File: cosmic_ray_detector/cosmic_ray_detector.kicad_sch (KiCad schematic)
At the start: 10 parts, among them J2 5 pin pin header, J3 Black Banana, J5 Green Banana, J6 BNC

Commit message: many more footprints coming in
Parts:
- C1: value C -> (none)
- J2: value 5 pin pin header -> (none)
- J3: value Black Banana -> (none); Farnell (none) -> 1698983; MPN (none) -> 24.243.2; Manufacturer_Name (none) -> Multicomp
- J4: Farnell (none) -> 1698982; MPN (none) -> 24.243.1; Manufacturer_Name (none) -> Multicomp
- J5: value Green Banana -> (none); Farnell (none) -> 1698986; MPN (none) -> 24.243.4; Manufacturer_Name (none) -> Multicomp
- J6: value BNC -> (none); Farnell (none) -> 1076289; MPN (none) -> 6252H7-NPP3G-50; Manufacturer_Name (none) -> Amphenol
- L1, L2: value L -> (none)
- R1: value R_US -> (none)

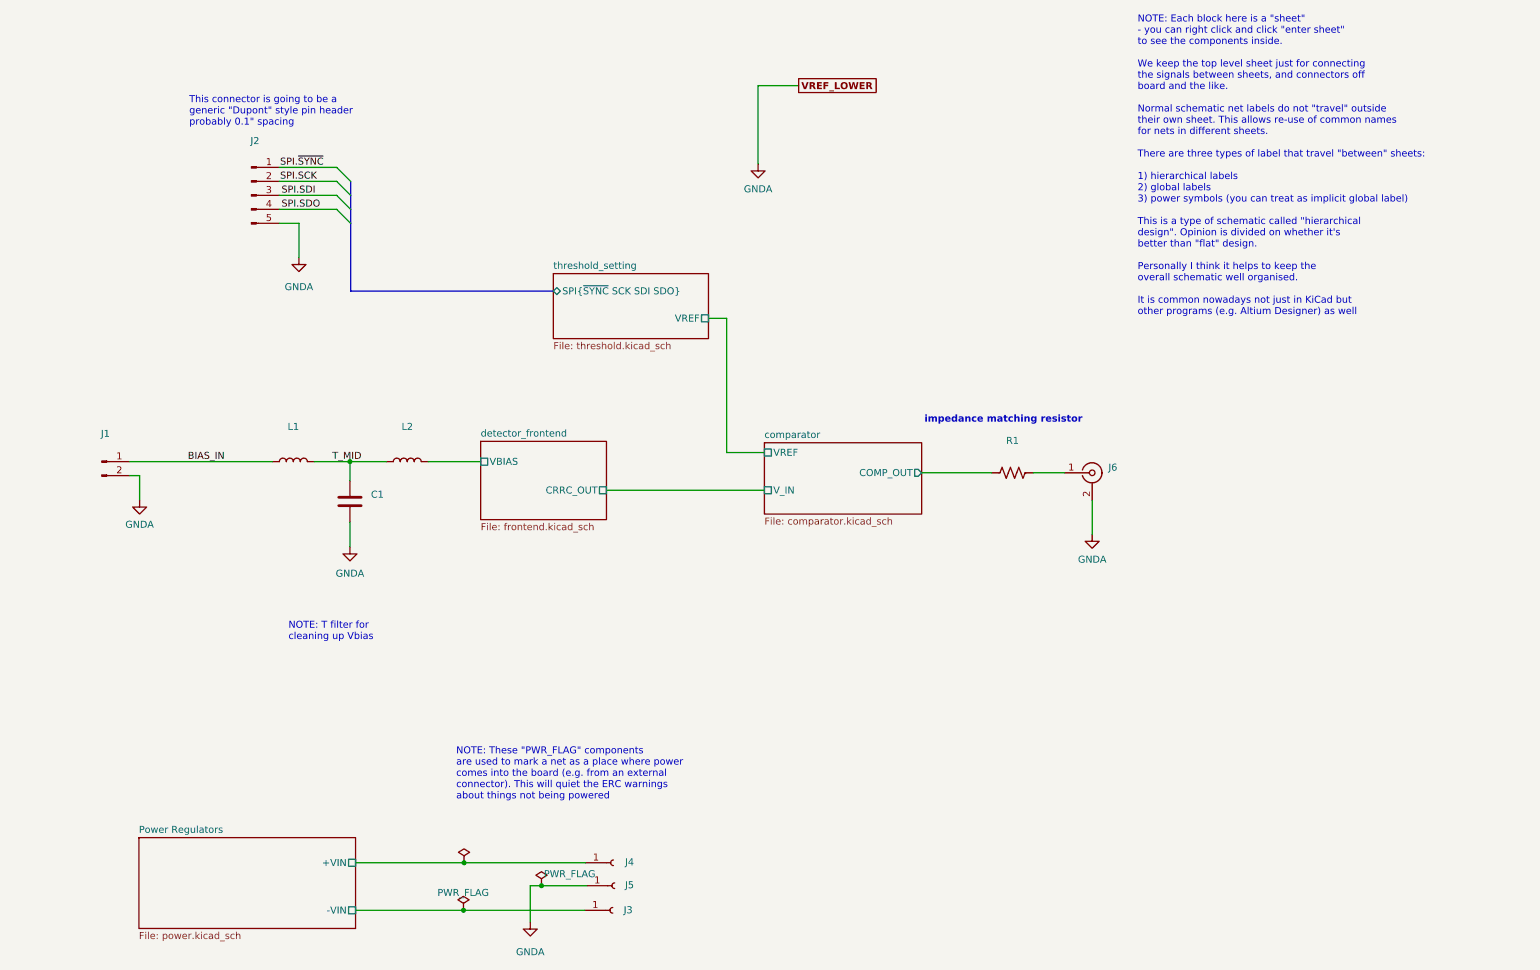
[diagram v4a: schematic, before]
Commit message: add conceptual design, tweaks to schematics
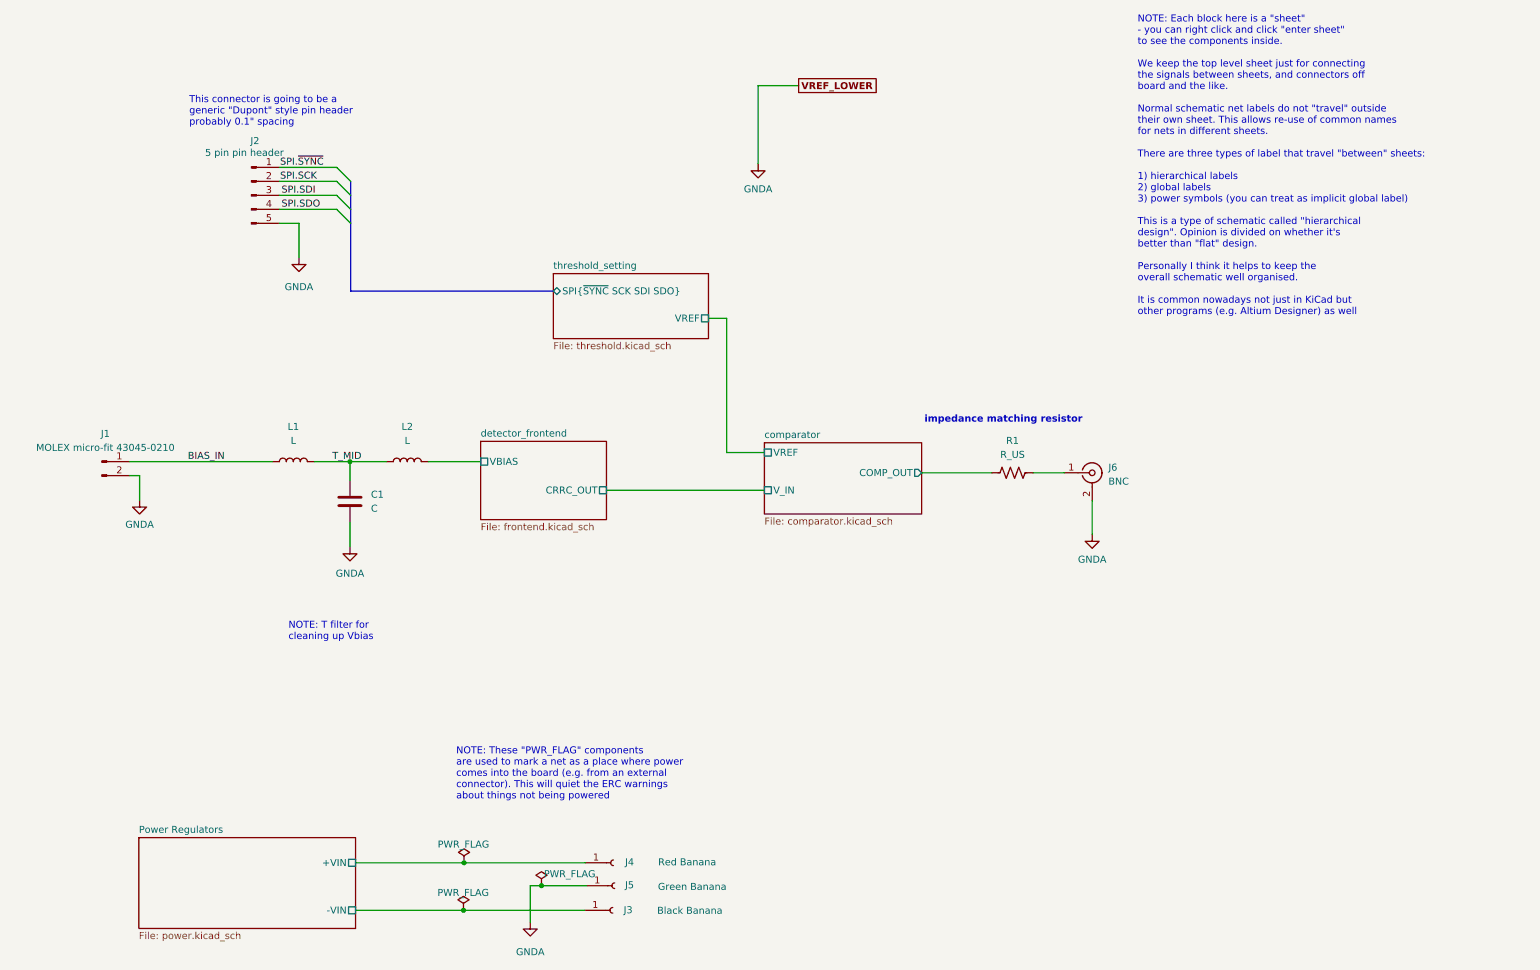
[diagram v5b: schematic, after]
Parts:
- C1: value (none) -> C; footprint (none) -> Capacitor_SMD:C_1210_3225Metric
- J1: value (none) -> MOLEX micro-fit 43045-0210; footprint (none) -> cosmic_ray_detector_lib:4304502_09
- J2: value (none) -> 5 pin pin header; footprint (none) -> Connector_PinHeader_1.27mm:PinHeader_1x05_P1.27mm_Vertical
- J3: value (none) -> Black Banana; footprint (none) -> cosmic_ray_detector_lib:242432
- J4: value (none) -> Red Banana; footprint (none) -> cosmic_ray_detector_lib:242431
- J5: value (none) -> Green Banana; footprint (none) -> cosmic_ray_detector_lib:242434
- J6: value (none) -> BNC; footprint (none) -> cosmic_ray_detector_lib:MOLEX_731375003
- L1, L2: value (none) -> L; footprint (none) -> Inductor_SMD:L_1008_2520Metric
- R1: value (none) -> R_US; footprint (none) -> Resistor_SMD:R_0402_1005Metric
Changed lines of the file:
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@@
     (in_bom yes) (on_board yes)
     (property "Reference" "J2" (id 0) (at 63.754 37.719 0))
-    (property "Value" "" (id 1) (at 61.849 39.878 0))
-    (property "Footprint" "" (id 2) (at 63.119 47.625 0)
+    (property "Value" "5 pin pin header" (id 1) (at 61.849 39.878 0))
+    (property "Footprint" "Connector_PinHeader_1.27mm:PinHeader_1x05_P1.27mm_Vertical" (id 2) (at 63.119 47.625 0)
       (effects (font (size 1.27 1.27)) hide)
     )
@@
       (effects (font (size 1.27 1.27)) (justify right))
     )
-    (property "Value" "" (id 1) (at 84.836 104.5209 0)
+    (property "Value" "C" (id 1) (at 84.836 104.5209 0)
       (effects (font (size 1.27 1.27)) (justify right))
     )
-    (property "Footprint" "" (id 2) (at 80.0608 99.441 0)
+    (property "Footprint" "Capacitor_SMD:C_1210_3225Metric" (id 2) (at 80.0608 99.441 0)
       (effects (font (size 1.27 1.27)) hide)
     )
@@
       (effects (font (size 1.27 1.27)) (justify left))
     )
-    (property "Value" "" (id 1) (at 218.8464 99.6071 0)
-      (effects (font (size 1.27 1.27)) (justify left))
-    )
-    (property "Footprint" "" (id 2) (at 215.9 98.044 0)
+    (property "Value" "BNC" (id 1) (at 218.8464 99.6071 0)
+      (effects (font (size 1.27 1.27)) (justify left))
+    )
+    (property "Footprint" "cosmic_ray_detector_lib:MOLEX_731375003" (id 2) (at 215.9 98.044 0)
       (effects (font (size 1.27 1.27)) hide)
     )
@@
     (in_bom yes) (on_board yes) (fields_autoplaced)
     (property "Reference" "L1" (id 0) (at 70.739 89.662 90))
-    (property "Value" "" (id 1) (at 70.739 92.202 90))
-    (property "Footprint" "" (id 2) (at 70.739 96.012 0)
+    (property "Value" "L" (id 1) (at 70.739 92.202 90))
+    (property "Footprint" "Inductor_SMD:L_1008_2520Metric" (id 2) (at 70.739 96.012 0)
       (effects (font (size 1.27 1.27)) hide)
     )
@@
       (effects (font (size 1.27 1.27)) hide)
     )
-    (property "Value" "" (id 1) (at 101.6508 165.5572 0))
+    (property "Value" "PWR_FLAG" (id 1) (at 101.6508 165.5572 0))
     (property "Footprint" "" (id 2) (at 101.7524 168.91 0)
       (effects (font (size 1.27 1.27)) hide)
@@
       (effects (font (size 1.27 1.27)) (justify left))
     )
-    (property "Value" "" (id 1) (at 137.033 168.783 0)
-      (effects (font (size 1.27 1.27)) (justify left))
-    )
-    (property "Footprint" "" (id 2) (at 128.905 168.91 0)
+    (property "Value" "Red Banana" (id 1) (at 137.033 168.783 0)
+      (effects (font (size 1.27 1.27)) (justify left))
+    )
+    (property "Footprint" "cosmic_ray_detector_lib:242431" (id 2) (at 128.905 168.91 0)
       (effects (font (size 1.27 1.27)) hide)
     )
@@
     (in_bom yes) (on_board yes) (fields_autoplaced)
     (property "Reference" "J1" (id 0) (at 36.576 90.932 0))
-    (property "Value" "" (id 1) (at 36.576 93.472 0))
-    (property "Footprint" "" (id 2) (at 35.941 96.012 0)
+    (property "Value" "MOLEX micro-fit 43045-0210" (id 1) (at 36.576 93.472 0))
+    (property "Footprint" "cosmic_ray_detector_lib:4304502_09" (id 2) (at 35.941 96.012 0)
       (effects (font (size 1.27 1.27)) hide)
     )
@@
     (in_bom yes) (on_board yes) (fields_autoplaced)
     (property "Reference" "L2" (id 0) (at 91.44 89.662 90))
-    (property "Value" "" (id 1) (at 91.44 92.202 90))
-    (property "Footprint" "" (id 2) (at 91.44 96.012 0)
+    (property "Value" "L" (id 1) (at 91.44 92.202 90))
+    (property "Footprint" "Inductor_SMD:L_1008_2520Metric" (id 2) (at 91.44 96.012 0)
       (effects (font (size 1.27 1.27)) hide)
     )
@@
       (effects (font (size 1.27 1.27)) (justify left))
     )
-    (property "Value" "" (id 1) (at 136.9822 173.2534 0)
-      (effects (font (size 1.27 1.27)) (justify left))
-    )
-    (property "Footprint" "" (id 2) (at 129.1336 173.0756 0)
+    (property "Value" "Green Banana" (id 1) (at 136.9822 173.2534 0)
+      (effects (font (size 1.27 1.27)) (justify left))
+    )
+    (property "Footprint" "cosmic_ray_detector_lib:242434" (id 2) (at 129.1336 173.0756 0)
       (effects (font (size 1.27 1.27)) hide)
     )
@@
       (effects (font (size 1.27 1.27)) (justify left))
     )
-    (property "Value" "" (id 1) (at 136.8552 177.5968 0)
-      (effects (font (size 1.27 1.27)) (justify left))
-    )
-    (property "Footprint" "" (id 2) (at 128.778 177.546 0)
+    (property "Value" "Black Banana" (id 1) (at 136.8552 177.5968 0)
+      (effects (font (size 1.27 1.27)) (justify left))
+    )
+    (property "Footprint" "cosmic_ray_detector_lib:242432" (id 2) (at 128.778 177.546 0)
       (effects (font (size 1.27 1.27)) hide)
     )
@@
     (in_bom yes) (on_board yes) (fields_autoplaced)
     (property "Reference" "R1" (id 0) (at 201.422 92.202 90))
-    (property "Value" "" (id 1) (at 201.422 94.742 90))
-    (property "Footprint" "" (id 2) (at 201.676 97.028 90)
+    (property "Value" "R_US" (id 1) (at 201.422 94.742 90))
+    (property "Footprint" "Resistor_SMD:R_0402_1005Metric" (id 2) (at 201.676 97.028 90)
       (effects (font (size 1.27 1.27)) hide)
     )
@@
     )
     (path "/5d423df9-0691-4d6c-a6f8-df6ce27066a8/65278bfc-14d1-478b-8143-85b3c07e62c3"
-      (reference "U5") (unit 1) (value "AD5270BRMZ-100-RL7") (footprint "SOP50P490X110-10N")
-    )
-  )
+      (reference "U5") (unit 1) (value "AD5270BRMZ-100-RL7") (footprint "cosmic_ray_detector_lib:SOP50P490X110-10N")
+    )
+  )

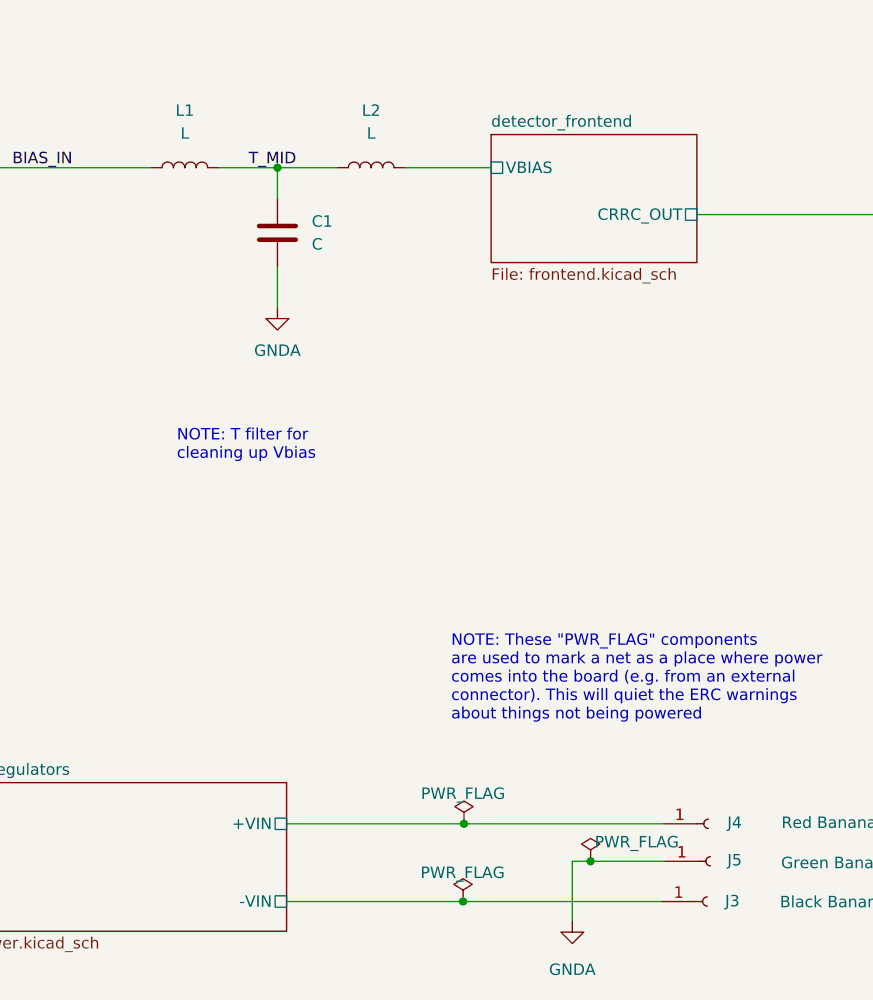
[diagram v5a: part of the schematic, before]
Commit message: update schematic complete to v8
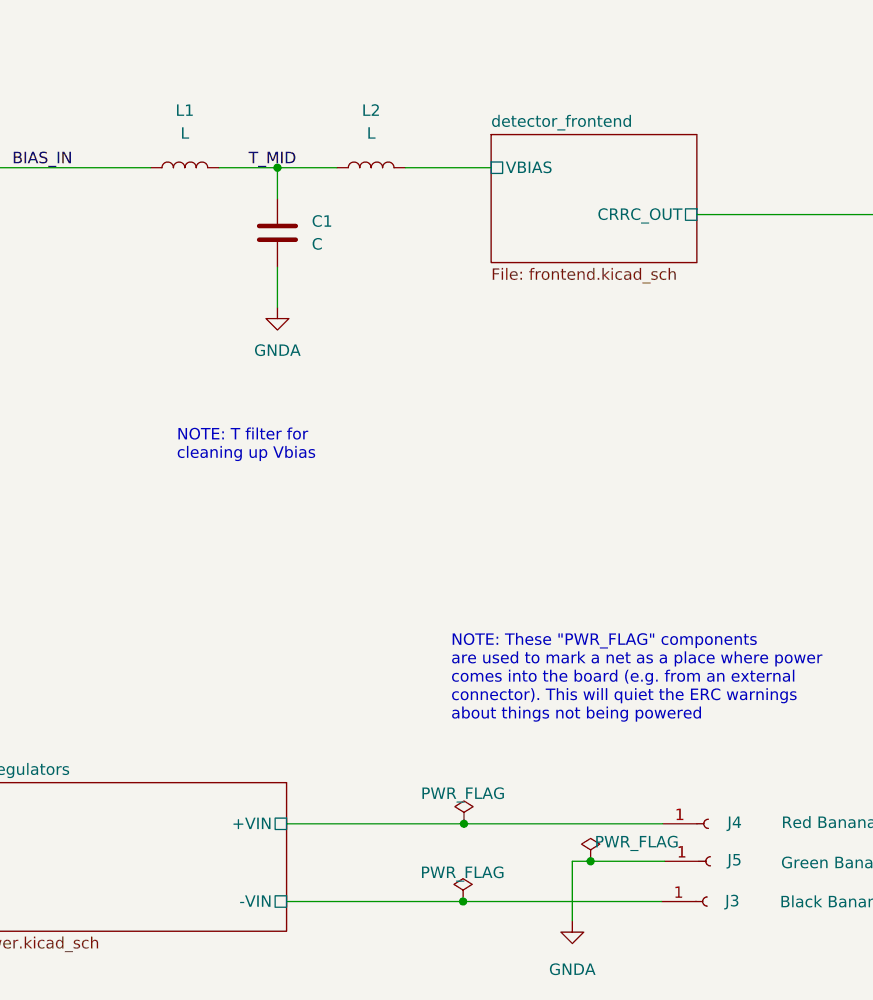
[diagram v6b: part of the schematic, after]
